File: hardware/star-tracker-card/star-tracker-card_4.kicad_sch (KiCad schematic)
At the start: 42 parts, among them J102 FTSH-105-XX-X-DV-K, U1 RCLAMP0504FB, U2 TPS2051CDBVR, U7 OSD3358-512M-BSM, Y1 24MHz, Y2 ABS07-32.768KHZ-T

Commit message: More EAGLE import cleanup
Fixed sheets, did some ERC cleanup, imported into layout, impmorted 4 layer DRC rules.
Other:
- note removed: "1.2"
- note removed: "OreSat Star Tracker: USB, JTAG, OSC"
- company: (none) -> Portland State Aerospace Society
- title: (none) -> OreSat Star Tracker
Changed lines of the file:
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@@
 	(generator "eeschema")
 	(generator_version "9.0")
-	(paper "User" 469.9 317.627)
+	(paper "B")
+	(title_block
+		(title "OreSat Star Tracker")
+		(date "2026-01-30")
+		(rev "1.3")
+		(company "Portland State Aerospace Society")
+	)
 	(text "USB ESD\nprotection"
 		(exclude_from_sim no)
@@
 	(text "1M if populated"
 		(exclude_from_sim no)
-		(at 170.688 92.456 0)
+		(at 170.18 92.71 0)
 		(effects
 			(font
@@
 		)
 	)
-	(text "OreSat Star Tracker: USB, JTAG, OSC"
-		(exclude_from_sim no)
-		(at 349.25 270.51 0)
-		(effects
-			(font
-				(size 3.81 3.2385)
-			)
-			(justify left bottom)
-		)
-	)
-	(text "1.2"
-		(exclude_from_sim no)
-		(at 433.07 290.83 0)
-		(effects
-			(font
-				(size 3.81 3.2385)
-			)
-			(justify left bottom)
-		)
-	)
 	(text "taken verbatim from PB,"
 		(exclude_from_sim no)
@@
 	(text "24MHz RTC XO"
 		(exclude_from_sim no)
-		(at 91.694 63.246 0)
+		(at 91.44 63.5 0)
 		(effects
 			(font
@@
 	(text "USB Power Switch"
 		(exclude_from_sim no)
-		(at 297.815 191.135 0)
+		(at 298.45 191.77 0)
 		(effects
 			(font
@@
 	(text "USB Client Circuit"
 		(exclude_from_sim no)
-		(at 179.578 177.038 0)
+		(at 179.07 176.53 0)
 		(effects
 			(font
@@
 	(polyline
 		(pts
-			(xy 111.76 182.88) (xy 111.76 176.276)
+			(xy 111.76 182.88) (xy 111.76 176.53)
 		)
 		(stroke
@@
 	(polyline
 		(pts
-			(xy 111.76 176.276) (xy 162.56 176.276)
+			(xy 111.76 176.53) (xy 162.56 176.53)
 		)
 		(stroke
@@
 	(polyline
 		(pts
-			(xy 162.56 176.276) (xy 162.56 182.88)
+			(xy 162.56 176.53) (xy 162.56 182.88)
 		)
 		(stroke
@@
 	)
 	(symbol
-		(lib_id "star-tracker-card-eagle-import:frames_229_FRAME_B_L")
-		(at 342.9 297.18 0)
-		(unit 2)
-		(exclude_from_sim no)
-		(in_bom yes)
-		(on_board yes)
-		(dnp no)
-		(property "Reference" "#FRAME4"
-			(at 342.9 297.18 0)
-			(effects
-				(font
-					(size 1.27 1.27)
-				)
-				(hide yes)
-			)
-		)
-		(property "Value" "FRAME_B_L"
-			(at 342.9 297.18 0)
-			(effects
-				(font
-					(size 1.27 1.27)
-				)
-				(hide yes)
-			)
-		)
-		(property "Footprint" ""
-			(at 342.9 297.18 0)
-			(effects
-				(font
-					(size 1.27 1.27)
-				)
-				(hide yes)
-			)
-		)
-		(property "Datasheet" ""
-			(at 342.9 297.18 0)
-			(effects
-				(font
-					(size 1.27 1.27)
-				)
-				(hide yes)
-			)
-		)
-		(property "Description" ""
-			(at 342.9 297.18 0)
-			(effects
-				(font
-					(size 1.27 1.27)
-				)
-				(hide yes)
-			)
-		)
-		(instances
-			(project ""
-				(path "/324e9eb5-7420-4b7e-862c-cc20bb28618a/180c7308-0a0c-41f6-9c76-108b10aa05c2"
-					(reference "#FRAME4")
-					(unit 2)
-				)
-			)
-		)
-	)
-	(symbol
 		(lib_id "star-tracker-card-eagle-import:TEST-POINT3X4")
 		(at 251.46 129.54 0)
@@
 					(unit 1)
 				)
-			)
-		)
-	)
-	(symbol
-		(lib_id "star-tracker-card-eagle-import:frames_229_FRAME_B_L")
-		(at 17.78 297.18 0)
-		(unit 1)
-		(exclude_from_sim no)
-		(in_bom yes)
-		(on_board yes)
-		(dnp no)
-		(property "Reference" "#FRAME4"
-			(at 17.78 297.18 0)
-			(effects
-				(font
-					(size 1.27 1.27)
-				)
-				(hide yes)
-			)
-		)
-		(property "Value" "FRAME_B_L"
-			(at 17.78 297.18 0)
-			(effects
-				(font
-					(size 1.27 1.27)
-				)
-				(hide yes)
-			)
-		)
-		(property "Footprint" ""
-			(at 17.78 297.18 0)
-			(effects
-				(font
-					(size 1.27 1.27)
-				)
-				(hide yes)
-			)
-		)
-		(property "Datasheet" ""
-			(at 17.78 297.18 0)
-			(effects
-				(font
-					(size 1.27 1.27)
-				)
-				(hide yes)
-			)
-		)
-		(property "Description" ""
-			(at 17.78 297.18 0)
-			(effects
-				(font
-					(size 1.27 1.27)
-				)
-				(hide yes)
-			)
-		)
-		(instances
-			(project ""
-				(path "/324e9eb5-7420-4b7e-862c-cc20bb28618a/180c7308-0a0c-41f6-9c76-108b10aa05c2"
-					(reference "#FRAME4")
-					(unit 1)
-				)

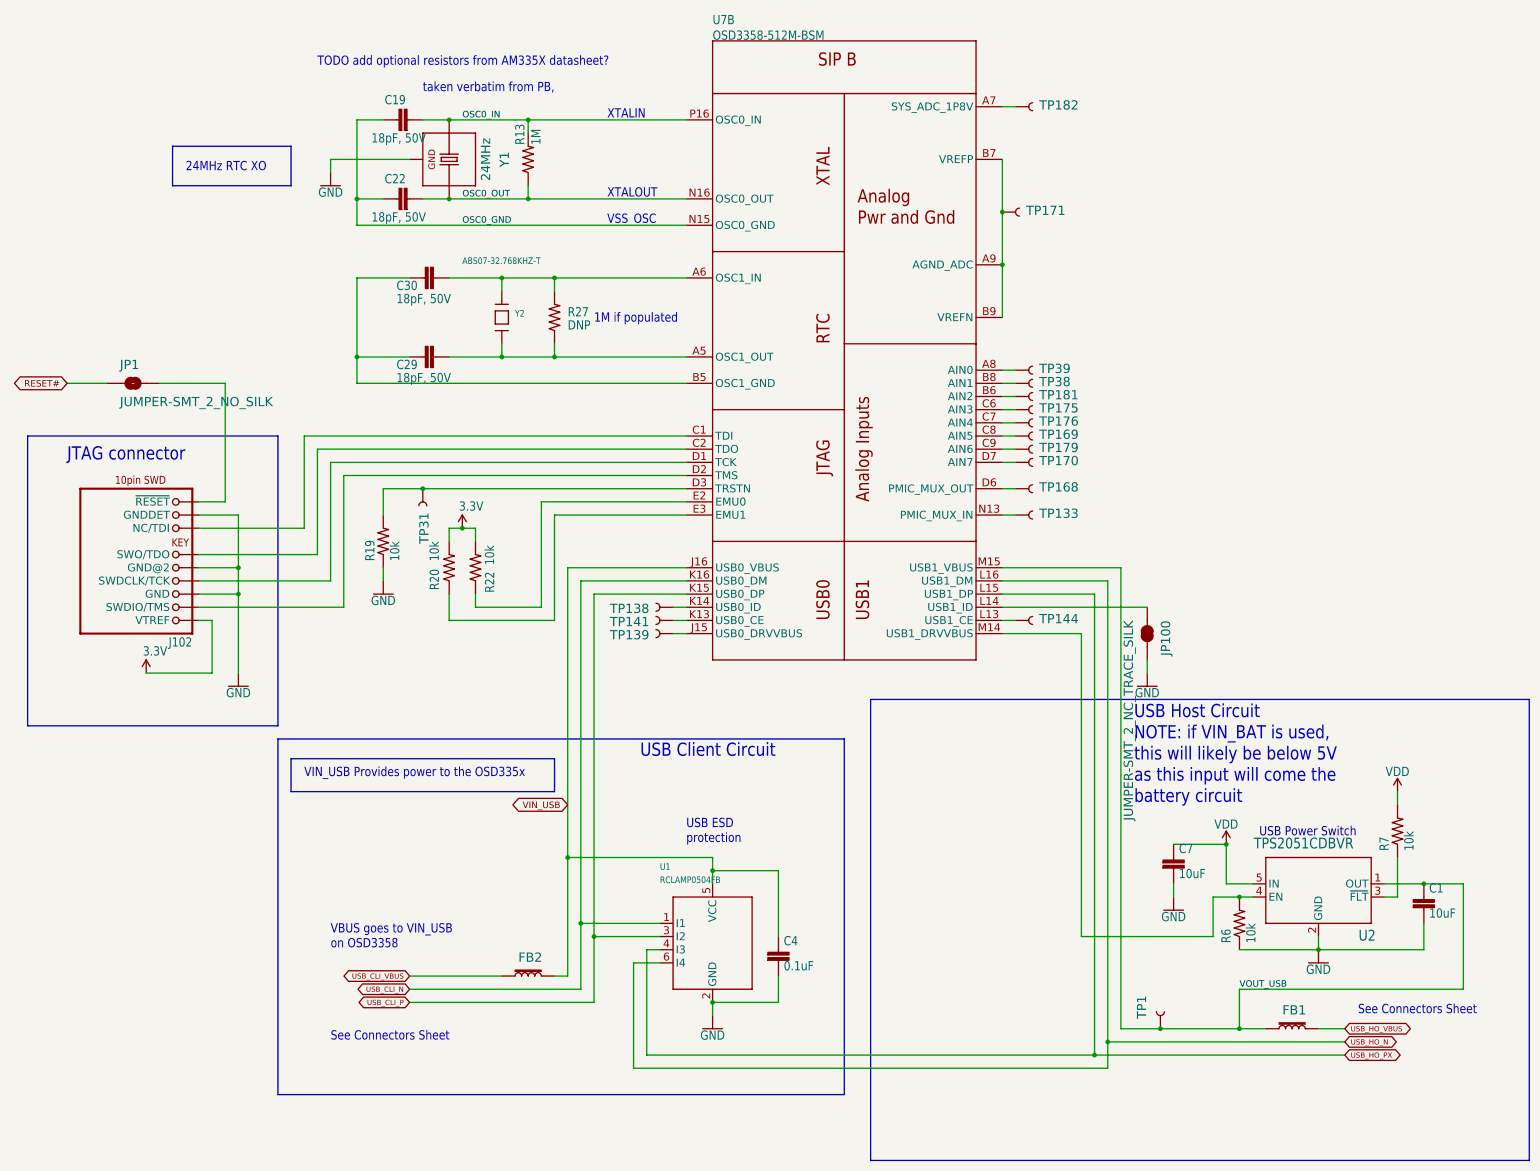
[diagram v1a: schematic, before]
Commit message: Schematic Overhaul of v1.3
Changed schematic to hierarchical, changed debug connector, updated OPD, removed JTAG, and ESD protection on removed connectors
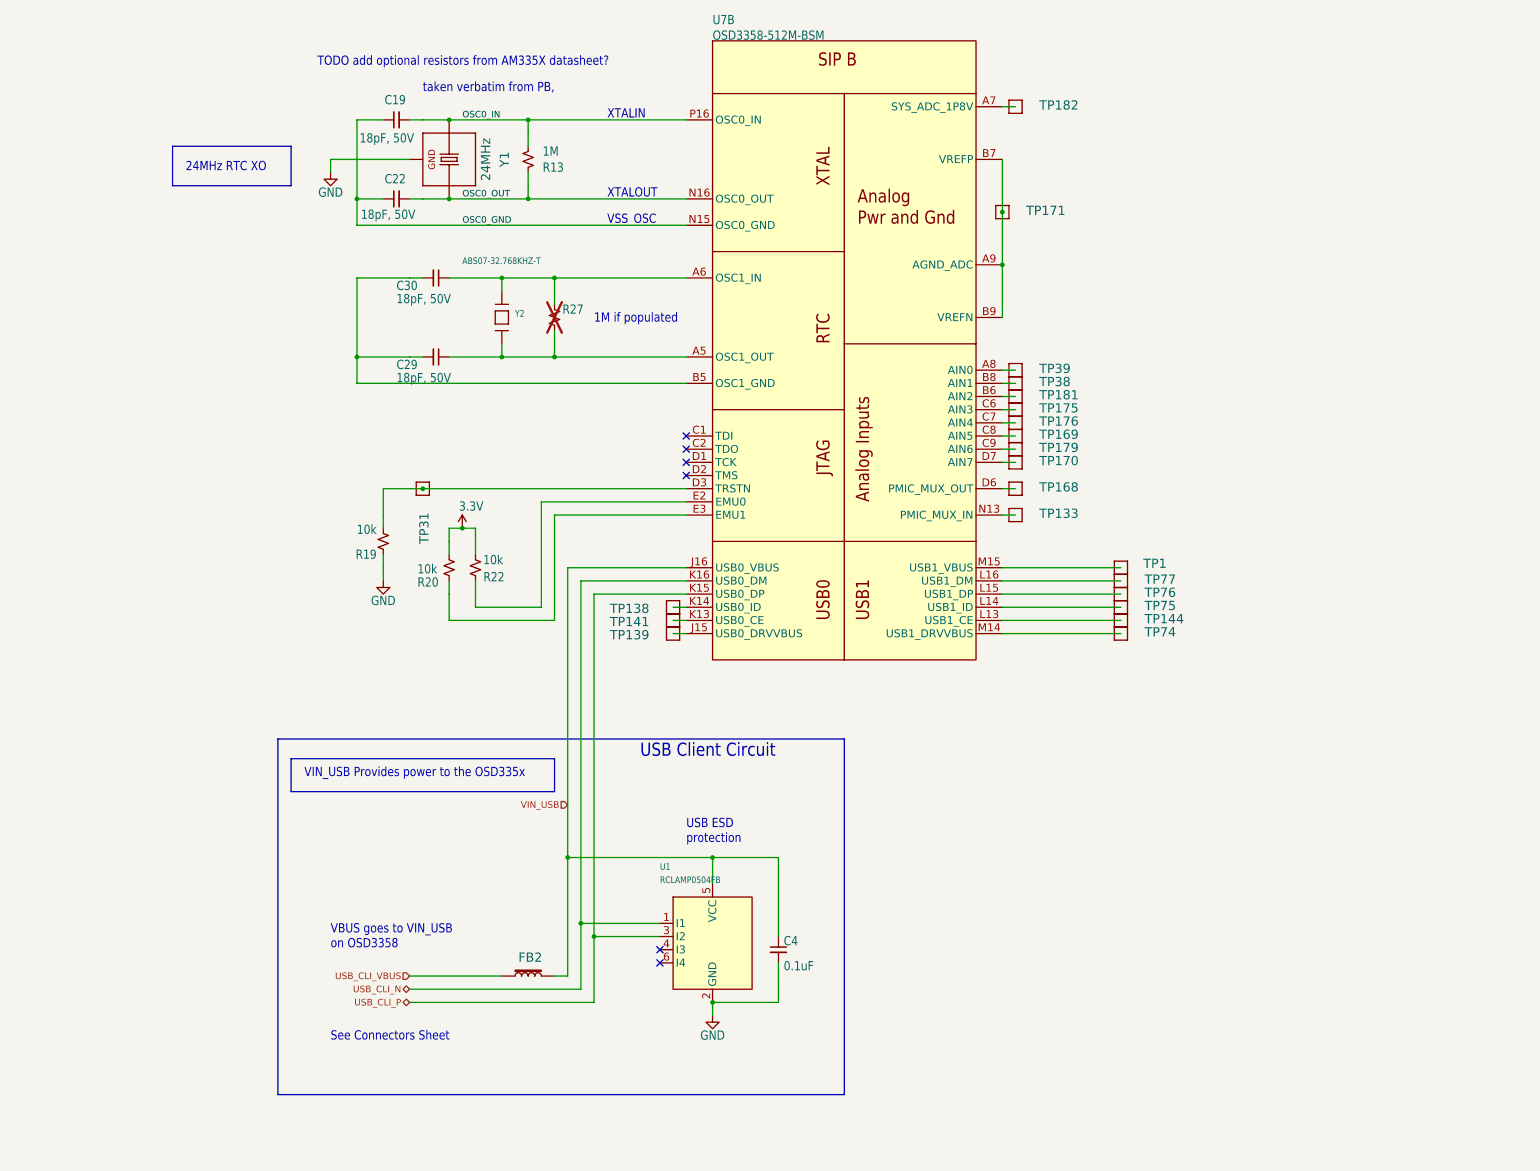
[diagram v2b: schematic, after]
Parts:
- removed C1, C7: 10uF, star-tracker-card:.0805-B, symbol star-tracker-card-eagle-import:C-EU0805-B
- removed FB1: 30Ω/1.8A, star-tracker-card:0603, symbol star-tracker-card-eagle-import:FERRITE_BEAD-0603
- removed J102: FTSH-105-XX-X-DV-K, star-tracker-card:CON10_2X5_DUK_FTSH, symbol star-tracker-card-eagle-import:FTSH-105-XX-X-DV-K
- removed JP1: JUMPER-SMT_2_NO_SILK, star-tracker-card:SMT-JUMPER_2_NO_SILK, symbol star-tracker-card-eagle-import:JUMPER-SMT_2_NO_SILK
- removed JP100: JUMPER-SMT_2_NC_TRACE_SILK, star-tracker-card:SMT-JUMPER_2_NC_TRACE_SILK, symbol star-tracker-card-eagle-import:JUMPER-SMT_2_NC_TRACE_SILK
- removed R6, R7: 10k, star-tracker-card:.0603-A, symbol star-tracker-card-eagle-import:R-US_0603-A
- removed U2: TPS2051CDBVR, star-tracker-card:DBV5, symbol star-tracker-card-eagle-import:TPS2051CDBVR
- added TP74, TP75, TP76, TP77: TEST-POINT3X4, oresat-misc:TestPoint_Pad_D1.0mm, symbol oresat-misc:Test-Point-1mm-round
- C19, C22, C29, C30, C4: footprint star-tracker-card:.0603-A -> oresat-passives:c_0603-SMALL; symbol star-tracker-card-eagle-import:C-EU0603-A -> Device:C_Small
- R13, R19, R20, R22: footprint star-tracker-card:.0603-A -> Resistor_SMD:R_0603_1608Metric; symbol star-tracker-card-eagle-import:R-US_0603-A -> Device:R_Small_US
- R27: footprint star-tracker-card:.0603-A -> Resistor_SMD:R_0603_1608Metric; symbol star-tracker-card-eagle-import:R-US_0603-A -> Device:R_Small_US; now not fitted
- TP1, TP133, TP138, TP139, TP141, TP144, TP168, TP169, TP170, TP171, TP175, TP176, TP179, TP181, TP182, TP31, TP38, TP39: footprint star-tracker-card:PAD.03X.04 -> oresat-misc:TestPoint_Pad_D1.0mm; symbol star-tracker-card-eagle-import:TEST-POINT3X4 -> oresat-misc:Test-Point-1mm-round; now left out of the parts list
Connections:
- net at U7.D6 (PMIC_MUX_OUT): now also TP168.1; no longer TP168.P$1 (1)
- net at U7.B8 (AIN1): now also TP38.1; no longer TP38.P$1 (1)
- net at U7.A9 (AGND_ADC), U7.B7 (VREFP), U7.B9 (VREFN): now also TP171.1; no longer TP171.P$1 (1)
- net at U7.A7 (SYS_ADC_1P8V): now also TP182.1; no longer TP182.P$1 (1)
- net at U7.C6 (AIN3): now also TP175.1; no longer TP175.P$1 (1)
- net at U7.K13 (USB0_CE): now also TP141.1; no longer TP141.P$1 (1)
- net at U7.D7 (AIN7): now also TP170.1; no longer TP170.P$1 (1)
- net at U7.N13 (PMIC_MUX_IN): now also TP133.1; no longer TP133.P$1 (1)
- net at U7.C7 (AIN4): now also TP176.1; no longer TP176.P$1 (1)
- net at U7.L14 (USB1_ID): now also TP75.1
- net at U7.A8 (AIN0): now also TP39.1; no longer TP39.P$1 (1)
- net at R19.2, U7.D3 (TRSTN): now also TP31.1; no longer TP31.P$1 (1)
- net at U7.M14 (USB1_DRVVBUS): now also TP74.1
- net at U7.C9 (AIN6): now also TP179.1; no longer TP179.P$1 (1)
- net at U7.J15 (USB0_DRVVBUS): now also TP139.1; no longer TP139.P$1 (1)
- net at U7.B6 (AIN2): now also TP181.1; no longer TP181.P$1 (1)
- net at U7.C8 (AIN5): now also TP169.1; no longer TP169.P$1 (1)
- net at U7.L13 (USB1_CE): now also TP144.1; no longer TP144.P$1 (1)
- net at U7.K14 (USB0_ID): now also TP138.1; no longer TP138.P$1 (1)
- net USB_HO_N: no longer names the net of U7.L16 (USB1_DM)
- net USB_HO_N: now also TP77.1; no longer U1.6 (I4)
- net USB_HO_PX: no longer names the net of U7.L15 (USB1_DP)
- net USB_HO_PX: now also TP76.1; no longer U1.4 (I3)
- net VOUT_USB: no longer names the net of U7.M15 (USB1_VBUS)
- net VOUT_USB: now also TP1.1; no longer TP1.P$1 (1)
- no-connect marks 0 -> 6
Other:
- note removed: "JTAG connector"
- note removed: "USB Host Circuit NOTE: if VIN_BAT is used, this will likely be below 5V as this input will come the battery circuit"
- note removed: "USB Power Switch"
